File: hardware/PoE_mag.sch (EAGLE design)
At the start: 124 parts, among them IC1 LD1117V33, IC10 PCA9517A, IC11 LD1117V33, IC2 DS1338, IC3 74LVC1T45SOT23-HAND, IC4 ATMEGA1284, IC5 MCP2200, IC6 TSR 1-2450, IC7 74LVC1T45SOT23-HAND, IC8 74LVC1T45SOT23-HAND, IC9 74LVC1T45SOT23-HAND, Q1 BSS138, Q3 BUK98150-55A, X1 PWR, X2 JTAG, X3 USB, X4 CONN-SMATHD, X5 UFL, X6 MICRO-SD-SOCKETHIROSE-DM3D, X7 RJ45, X8 RJ11, X9 22-23-2021, Y1 32k768, Y2 16MHz, Y3 12MHz

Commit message: Version before routing, and possible final routing
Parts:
- removed JP12: 5V LINK, SparkFun:JUMPER-2PTH
- removed JP13: MAG VCC, SparkFun:JUMPER-3PTH
- removed Q3: BUK98150-55A, SteveMarple:FET-N-TYPESOT223-HAND
- added JP2: ISP VCC, SparkFun:JUMPER-2PTH
- added JP3: SQW, SparkFun:JUMPER-3PTH
- added Q2: BUK98150-55A, SteveMarple:FET-N-TYPESOT223-HAND
- C10: value 22p -> 4u7; device SteveMarple:C-EU0805-HAND -> SparkFun:CAP_POLPTH2; OPTION Do not fit for ceramic resonator -> (none)
- C11: value 22p -> 100n; device SteveMarple:C-EU0805-HAND -> SteveMarple:C-EU1206-HAND; OPTION Do not fit for ceramic resonator -> (none)
- C12, C33, C36: value 100n -> 1u
- C13: value 10n -> 22p; device SteveMarple:C-EU1206-HAND -> SteveMarple:C-EU0805-HAND; OPTION (none) -> Do not fit for ceramic resonator
- C14: value 100n -> 22p; device SteveMarple:C-EU1206-HAND -> SteveMarple:C-EU0805-HAND; OPTION (none) -> Do not fit for ceramic resonator
- C15, C16, C21, C22, C28: value 22p -> 100n; device SteveMarple:C-EU0805-HAND -> SteveMarple:C-EU1206-HAND
- C17: value 15p -> 10n; device SteveMarple:C-EU0805-HAND -> SteveMarple:C-EU1206-HAND
- C18: value 15p -> 100n; device SteveMarple:C-EU0805-HAND -> SteveMarple:C-EU1206-HAND
- C19, C20, C34, C35: value 100n -> 22p; device SteveMarple:C-EU1206-HAND -> SteveMarple:C-EU0805-HAND
- C2: value 10u -> 1u; device SteveMarple:CAP_POLPTH2 -> SteveMarple:C-EU1206-HAND
- C27, C29, C39, C8: value 1u -> 100n
- C3: value 100n -> 10u; device SteveMarple:C-EU1206-HAND -> SteveMarple:CAP_POLPTH2
- C31: value 1u -> 22p; device SteveMarple:C-EU1206-HAND -> SteveMarple:C-EU0805-HAND
- C32: value 4u7 -> 1u; device SteveMarple:CAP_POLPTH2 -> SteveMarple:C-EU1206-HAND
- C37: value 100n -> 4u7; device SteveMarple:C-EU1206-HAND -> SteveMarple:CAP_POLPTH2
- C4: value 100p -> 15p; device SteveMarple:C-EU1206-HAND -> SteveMarple:C-EU0805-HAND
- C5: value 100n -> 15p; device SteveMarple:C-EU1206-HAND -> SteveMarple:C-EU0805-HAND
- C6: value 4u7 -> 100n; device SparkFun:CAP_POLPTH2 -> SteveMarple:C-EU1206-HAND
- C7: value 100n -> 100p
- D3: value BAS40 -> BAS21; device SteveMarple:DIODE-SCHOTTKYSOT23-1-3-HAND -> SteveMarple:DIODESOT23-1-3-HAND
- D4: value BAS21 -> BAS40; device SteveMarple:DIODESOT23-1-3-HAND -> SteveMarple:DIODE-SCHOTTKYSOT23-1-3-HAND
- IC1: device SteveMarple:V_REG_LD1117VXXTO220 -> SteveMarple:V_REG_LD1117VXXSOT223-HAND
- IC10: value PCA9517A -> 74LVC1T45SOT23-HAND; device SteveMarple:PCA9517ASOIC -> SteveMarple:74LVC1T45SOT23-HAND
- IC11: value LD1117V33 -> PCA9517A; device SteveMarple:V_REG_LD1117VXXSOT223-HAND -> SteveMarple:PCA9517ASOIC
- IC2: value DS1338 -> LD1117V33; device SteveMarple:DS1307SO08 -> SteveMarple:V_REG_LD1117VXXTO220
- IC3: value 74LVC1T45SOT23-HAND -> DS1338; device SteveMarple:74LVC1T45SOT23-HAND -> SteveMarple:DS1307SO08
- IC5: value MCP2200 -> TSR 1-2450; device SteveMarple:MCP2200 -> PoE_lib:V_REG_78XXTSR/POWERPAX
- IC6: value TSR 1-2450 -> MCP2200; device PoE_lib:V_REG_78XXTSR/POWERPAX -> SteveMarple:MCP2200
- JP1: value SQW -> 3V3/5V
- JP10: value CONFIG -> 5V LINK; device pinhead:PINHD-2X5 -> SparkFun:JUMPER-2PTH
- JP11: value GPS !RESET! (A0) -> MAG VCC; device SparkFun:JUMPER-2PTH -> SparkFun:JUMPER-3PTH
- JP4: value PPS -> USB/VIN
- JP5: value 3V3/5V -> AUTO RST; device SparkFun:JUMPER-3PTH -> SparkFun:JUMPER-2PTH
- JP6: value V ANT -> GPS !RESET! (A0); device SparkFun:JUMPER-3PTH -> SparkFun:JUMPER-2PTH
- JP7: value AUTO RST -> V ANT; device SparkFun:JUMPER-2PTH -> SparkFun:JUMPER-3PTH
- JP8: value ISP VCC -> CONFIG; device SparkFun:JUMPER-2PTH -> pinhead:PINHD-2X5
- JP9: value USB/VIN -> PPS
- R10: value 1M -> 1k
- R18: value 3k 1% -> 330R
- R19: value 1k 1% -> 1M
- R20: value 1M -> 3k 1%
- R21: value 330R -> 1k 1%
- R3: value 10k -> 1M
- R4: value 4k7 -> 10k
- R6: value 10k -> 4k7
- R7: value 1k -> 10k
- U$5: value ? -> PAD
- U$8: value PAD -> ?
- X4: value CONN-SMATHD -> MICRO-SD-SOCKETHIROSE-DM3D; device SteveMarple:CONN-SMATHD -> SteveMarple:MICRO-SD-SOCKETHIROSE-DM3D
- X5: value UFL -> CONN-SMATHD; device SteveMarple:CONN-UFLHAND -> SteveMarple:CONN-SMATHD
- X6: value MICRO-SD-SOCKETHIROSE-DM3D -> UFL; device SteveMarple:MICRO-SD-SOCKETHIROSE-DM3D -> SteveMarple:CONN-UFLHAND
- X7: value RJ45 -> 22-23-2021; device SteveMarple:RJ45-8PTH -> con-molex:22-23-2021
- X8: value RJ11 -> RJ45; device SteveMarple:RJ11-6PTH -> SteveMarple:RJ45-8PTH
- X9: value 22-23-2021 -> RJ11; device con-molex:22-23-2021 -> SteveMarple:RJ11-6PTH
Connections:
- net !GPS_RESET: now also IC7.A; no longer IC8.A
- net !MCP2200_RESET: now also IC6.!RST, R10.1; no longer IC5.!RST, R9.1
- net !RESET: now also C21.2, R7.1; no longer C12.2, R6.1
- net +3V3: now also C16.1, C3.+, C31.1, C32.1, C33.1, IC10.VCC_B, IC2.OUT, IC6.VUSB, JP1.1, JP11.3, JP7.3, JP8.2, JP8.4, JP8.6, U$3.1; no longer C19.1, C2.+, C25.1, C35.1, C36.1, IC11.OUT, IC3.VCC_B, IC5.VUSB, JP10.2, JP10.4, JP10.6, JP13.3, JP5.1, JP6.3, U$11.1
- net +5V: now also C2.1, IC2.IN, JP1.3, JP10.1, JP4.2, JP7.1, U$4.1; no longer C39.1, IC11.IN, JP12.1, JP5.3, JP6.1, JP9.2, U$12.1
- net +5V_USB: now also C17.1, JP4.3; no longer C13.1, JP9.3
- net 0(RX0): now also IC6.TX; no longer IC5.TX
- net 1(TX0): now also IC6.RX; no longer IC5.RX
- net 11(MOSI): now also X4.CMD; no longer X6.CMD
- net 12(MISO): now also X4.DAT0; no longer X6.DAT0
- net 13(SCK): now also R3.2, X4.CLK; no longer R10.2, X6.CLK
- net 15: now also JP3.1; no longer JP1.1
- net 20(SDA): now also IC11.SDA_A, IC3.SDA, R14.1, R6.1; no longer IC10.SDA_A, IC2.SDA, R15.1, R5.1
- net 21(SCL): now also IC11.SCL_A, IC3.SCL, R15.1, R5.1; no longer IC10.SCL_A, IC2.SCL, R14.1, R4.1
- net 22: now also X4.CD/DAT3; no longer X6.CD/DAT3
- net 3(TX1): now also IC8.B; no longer IC7.B
- net 6: now also JP3.3, JP9.3; no longer JP1.3, JP4.3
- net 7: now also JP9.1; no longer JP4.1
- net 8: now also R18.1; no longer R21.1
- net A0: now also JP6.1; no longer JP11.1
- net A2: now also D4.A, R20.2, R21.2; no longer D3.A, R18.2, R19.2
- net AREF: now also C8.1; no longer C5.1
- net AUTO_RESET: now also IC6.!RTS, JP5.1; no longer IC5.!RTS, JP7.1
- net AVCC: now also C11.1; no longer C9.1
- net FAN_CTRL: now also D3.C, Q2.D, X7-2.S; no longer D4.C, Q3.D, X9-2.S
- net GND: now also C10.-, C12.2, C2.2, C3.-, C32.2, C37.-, C6.2, D3.A, IC10.DIR, IC5.GND, IC6.VSS, JP8.10, JP8.8, Q2.S, R21.1, R3.1, U$2.1, X4.SHIELD, X4.VSS, X6.GND, X8.4, X9.2, X9.3; no longer C10.2, C2.-, C3.2, C32.-, C34.2, C37.2, C6.-, D4.A, IC3.DIR, IC5.VSS, IC6.GND, JP10.10, JP10.8, Q3.S, R10.1, R20.1, U$13.1, X4.GND, X6.SHIELD, X6.VSS, X7.3, X7.4, X8.2
- net GPIO0: now also U$6.1; no longer U$3.1
- net GPIO1: now also IC10.B, U$7.1; no longer IC9.B, U$4.1
- net GPIO2: now also U$8.1; no longer U$5.1
- net GPIO3: now also JP8.1, U$9.1; no longer JP10.1, U$6.1
- net GPIO4: now also JP8.3, U$10.1; no longer JP10.3, U$7.1
- net GPIO5: now also JP8.5, U$11.1; no longer JP10.5, U$8.1
- net GPIO6: now also JP8.7, U$12.1; no longer JP10.7, U$9.1
- net GPIO7: now also JP8.9, U$13.1; no longer JP10.9, U$10.1
- net GPS_RX1: now also IC8.A; no longer IC7.A
- net GPS_TX1: now also IC9.B; no longer IC3.B
- net MAG_SCL: now also IC11.SCL_B, X8.5, X9.4; no longer IC10.SCL_B, X7.5, X8.4
- net MAG_SDA: now also IC11.SDA_B, X8.7, X9.6; no longer IC10.SDA_B, X7.7, X8.6
- net MAG_VCC: now also C39.1, IC11.EN, IC11.VCC_B, JP10.2, X8.6, X9.5; no longer C37.1, IC10.EN, IC10.VCC_B, JP12.2, X7.6, X8.5
- net N$1: now also C14.1; no longer C11.1
- net N$11: now also C7.1, IC3.VBATT, R9.2; no longer C4.1, IC2.VBATT, R7.2
- net N$12: now also C5.1, IC3.X2; no longer C17.1, IC2.X2
- net N$14: now also IC5.OUT, JP4.1; no longer IC6.OUT, JP9.1
- net N$15: now also C21.1, JP5.2; no longer C12.1, JP7.2
- net N$18: now also C19.1, IC6.OSC1; no longer C15.1, IC5.OSC1
- net N$2: now also C13.1; no longer C10.1
- net N$22: now also IC7.B, JP6.2; no longer IC8.B, JP11.2
- net N$23: now also C34.2, X6.SIGNAL; no longer C21.2, X4.SIGNAL
- net N$24: now also C34.1; no longer C21.1
- net N$25: now also IC9.A; no longer IC3.A
- net N$26: now also JP11.2, X8.8; no longer JP13.2, X7.8
- net N$29: now also Q2.G, R18.2, R19.2; no longer Q3.G, R20.2, R21.2
- net N$5: now also C4.1, IC3.X1; no longer C18.1, IC2.X1
- net N$6: now also JP2.1; no longer JP8.1
- net N$7: now also C20.1, IC6.OSC2; no longer C16.1, IC5.OSC2
- net N$9: now also R9.1; no longer R7.1
- net PPS: now also IC10.A, JP9.2; no longer IC9.A, JP4.2
- net SLEEP_FLAG: now also U$5.1; no longer U$2.1
- net SQW: now also IC3.SQW, JP3.2, R4.1; no longer IC2.SQW, JP1.2, R3.1
- net USB_D+: now also IC6.D+; no longer IC5.D+
- net USB_D-: now also IC6.D-; no longer IC5.D-
- net VCC: now also C10.+, C15.1, C18.1, C22.1, C25.1, C6.1, C9.1, D4.C, IC11.VCC_A, IC3.VCC, IC6.VDD, JP1.2, JP2.2, R10.2, R7.2, X4.VDD; no longer C14.1, C20.1, C3.1, C33.1, C34.1, C6.+, C7.1, D3.C, IC2.VCC, IC3.VCC_A, IC5.VDD, JP5.2, JP8.2, R3.2, R9.2, X6.VDD
- net VIN: now also C12.1, IC5.IN, JP11.1, R20.1, X7-1.S, X8.2, X9.1; no longer C8.1, IC6.IN, JP13.1, R18.1, X7.2, X8.1, X9-1.S
- net V_ANT: now also C35.1, C36.1, C37.+, JP7.2; no longer C22.1, C31.1, C32.+, JP6.2
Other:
- note removed: "2.1"
- note removed: "TODO Add TO-220 option for LD-1117"
- note removed: "TODO Swap MCP1702 (3V3 and 5V) for SMD"

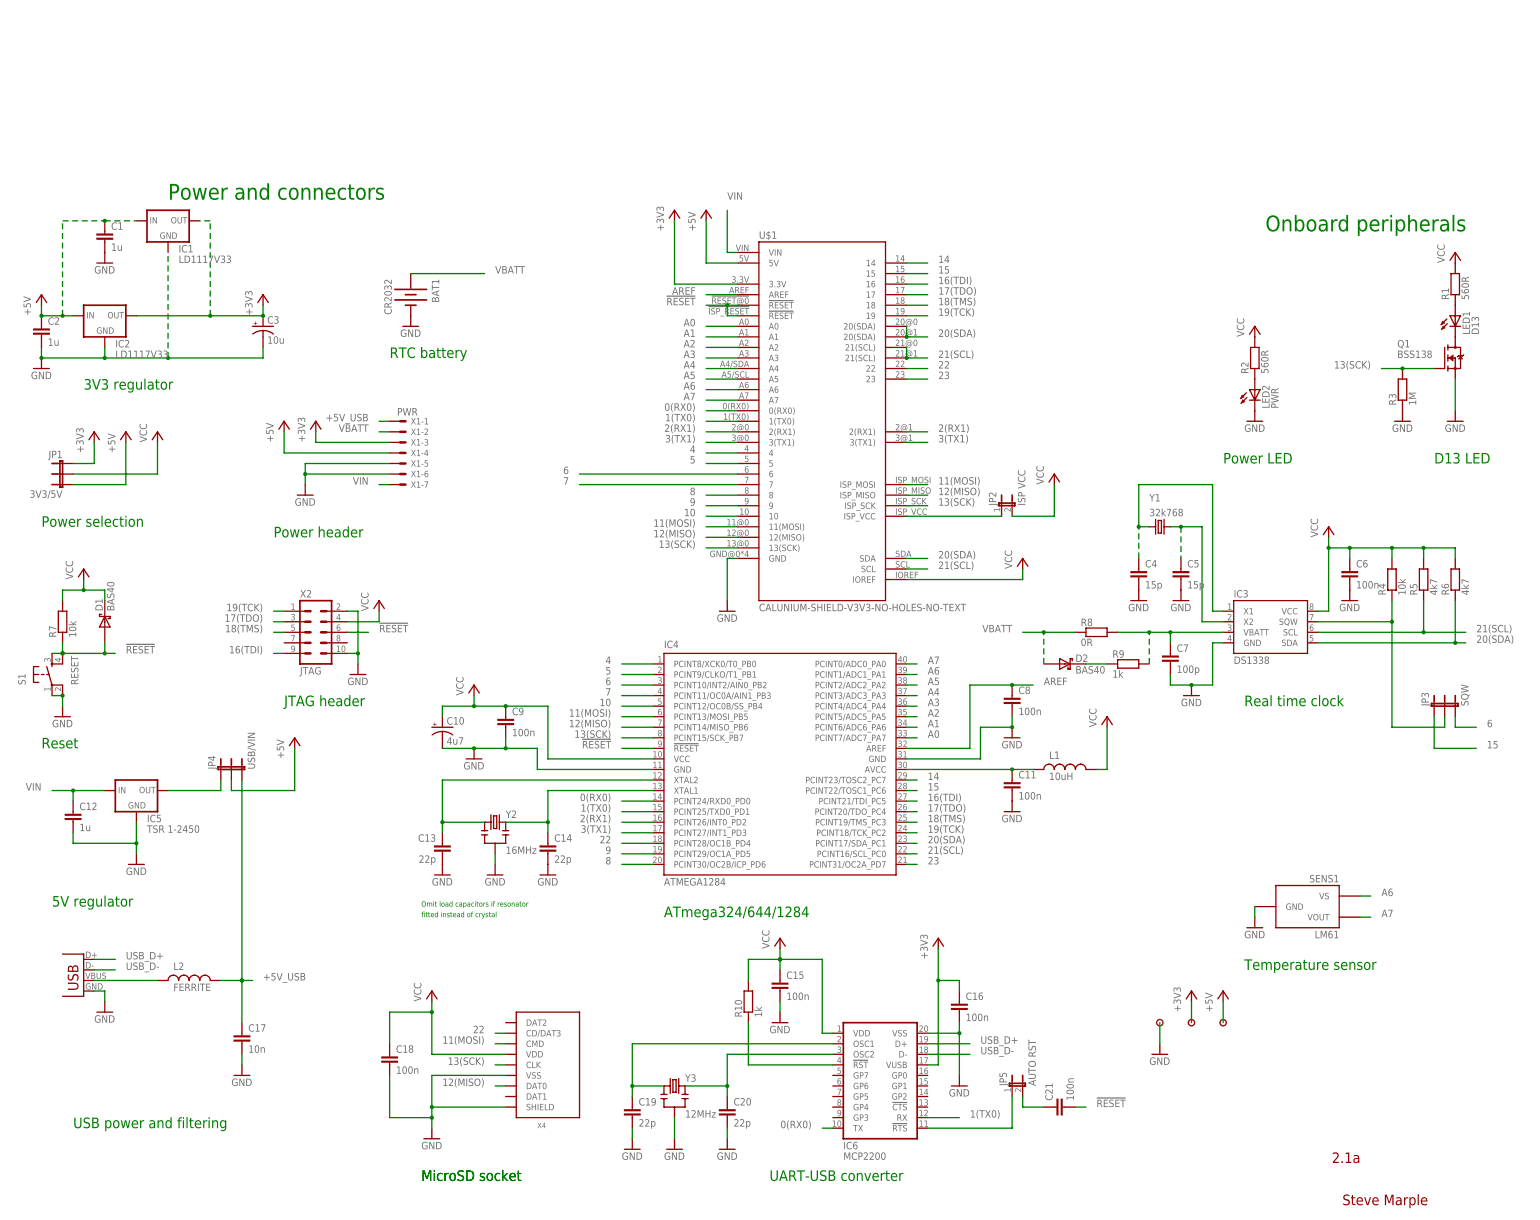
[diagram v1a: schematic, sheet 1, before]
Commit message: Fix incorrect USB power filtering
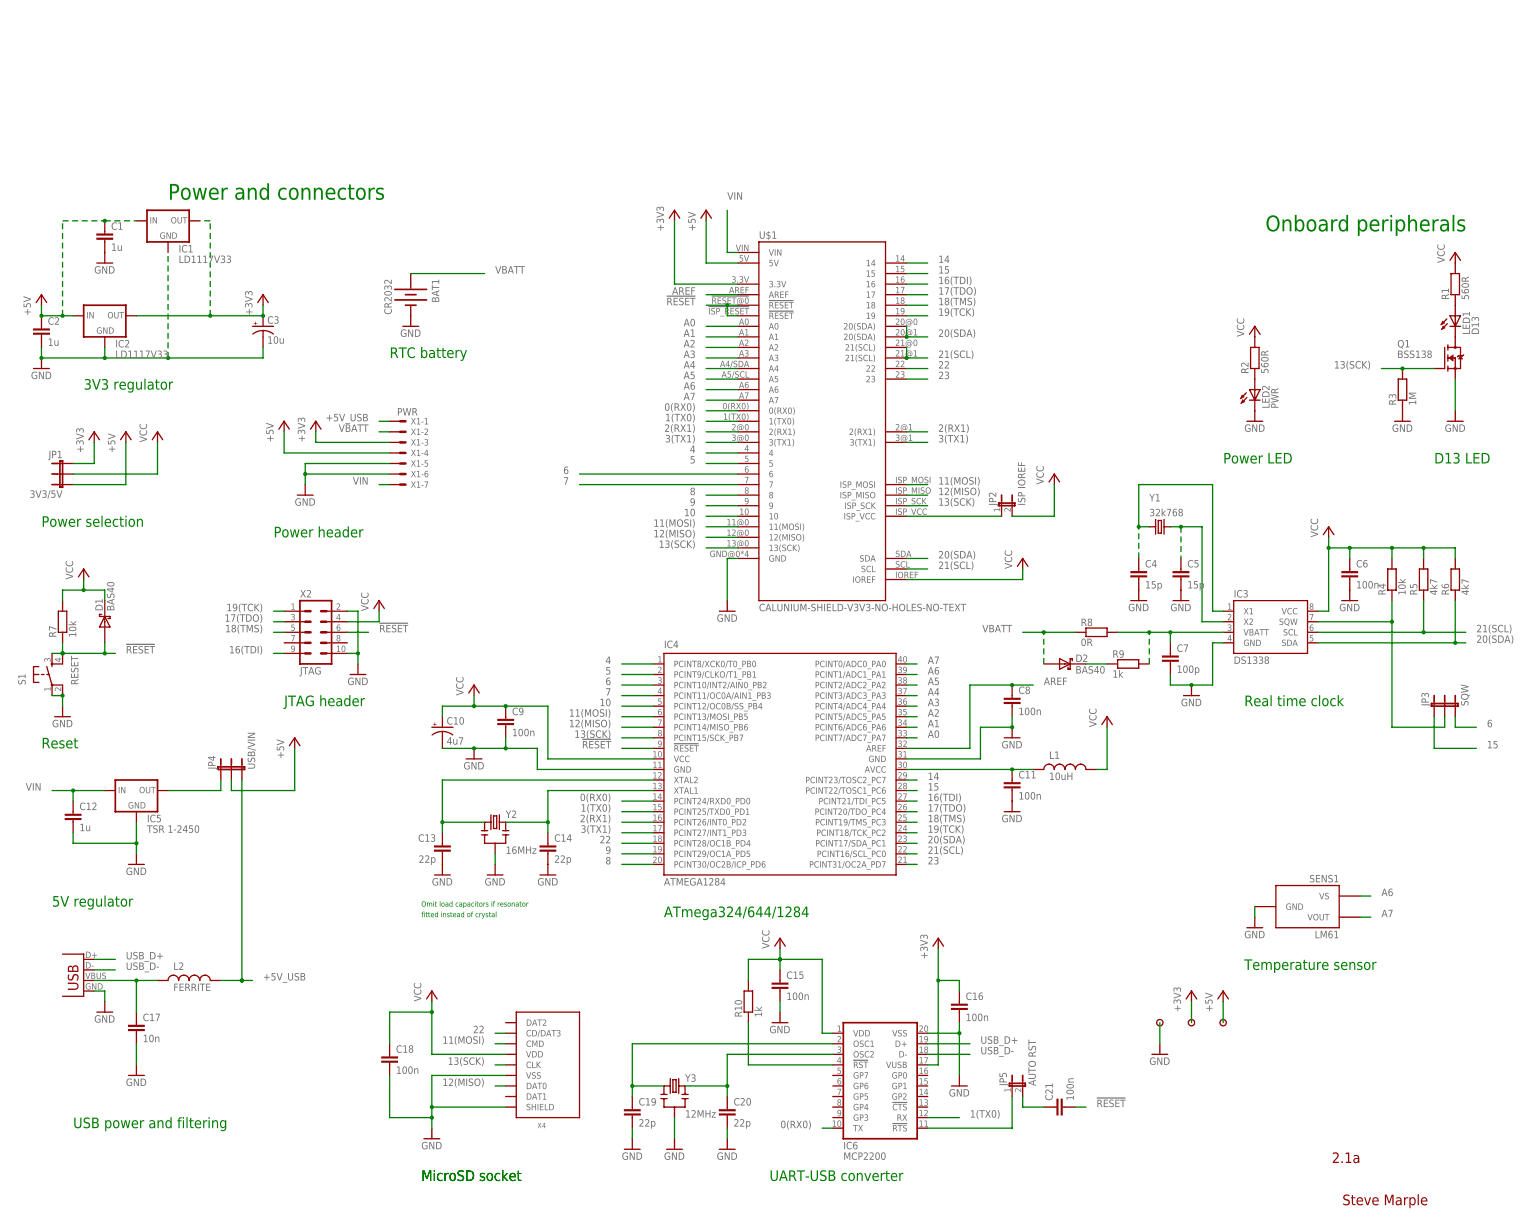
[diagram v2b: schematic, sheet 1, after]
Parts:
- JP2: value ISP VCC -> ISP IOREF
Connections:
- net +5V_USB: no longer C17.1
- net VBUS: now also C17.1
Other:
- moved on the sheet: C17
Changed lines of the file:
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@@
 <part name="P+23" library="supply1" deviceset="VCC" device=""/>
 <part name="GND32" library="supply1" deviceset="GND" device=""/>
-<part name="JP2" library="SparkFun" deviceset="JUMPER-2" device="PTH" value="ISP VCC"/>
+<part name="JP2" library="SparkFun" deviceset="JUMPER-2" device="PTH" value="ISP IOREF"/>
 <part name="JP3" library="SparkFun" deviceset="JUMPER-3" device="PTH" value="SQW"/>
 <part name="R8" library="SteveMarple" deviceset="RESISTOR" device="1206-HAND" value="0R"/>
@@
 <instance part="R8" gate="G$1" x="99.06" y="66.04"/>
 <instance part="L2" gate="G$1" x="-119.38" y="-17.78"/>
-<instance part="GND7" gate="1" x="-106.68" y="-40.64"/>
-<instance part="C17" gate="G$1" x="-106.68" y="-30.48"/>
+<instance part="GND7" gate="1" x="-132.08" y="-40.64"/>
+<instance part="C17" gate="G$1" x="-132.08" y="-27.94"/>
 <instance part="C16" gate="G$1" x="66.04" y="-22.86"/>
 <instance part="C15" gate="G$1" x="22.86" y="-17.78"/>
@@
 <pinref part="C17" gate="G$1" pin="2"/>
 <pinref part="GND7" gate="1" pin="GND"/>
-<wire x1="-106.68" y1="-38.1" x2="-106.68" y2="-35.56" width="0.1524" layer="91"/>
+<wire x1="-132.08" y1="-38.1" x2="-132.08" y2="-33.02" width="0.1524" layer="91"/>
 </segment>
 <segment>
@@
 <label x="-101.6" y="-17.78" size="1.778" layer="95"/>
 <junction x="-106.68" y="-17.78"/>
-<pinref part="C17" gate="G$1" pin="1"/>
-<wire x1="-106.68" y1="-27.94" x2="-106.68" y2="-17.78" width="0.1524" layer="91"/>
 <pinref part="JP4" gate="G$1" pin="3"/>
 <junction x="-106.68" y="-17.78"/>
@@
 </segment>
 </net>
-<net name="N$14" class="0">
+<net name="N$14" class="1">
 <segment>
 <pinref part="IC5" gate="G$1" pin="OUT"/>
@@
 <pinref part="X3" gate="G$1" pin="VBUS"/>
 <pinref part="L2" gate="G$1" pin="1"/>
-<wire x1="-127" y1="-17.78" x2="-142.24" y2="-17.78" width="0.1524" layer="91"/>
+<wire x1="-127" y1="-17.78" x2="-132.08" y2="-17.78" width="0.1524" layer="91"/>
+<junction x="-132.08" y="-17.78"/>
+<wire x1="-132.08" y1="-17.78" x2="-142.24" y2="-17.78" width="0.1524" layer="91"/>
+<pinref part="C17" gate="G$1" pin="1"/>
+<wire x1="-132.08" y1="-17.78" x2="-132.08" y2="-25.4" width="0.1524" layer="91"/>
 </segment>
 </net>
@@
 </segment>
 </net>
-<net name="MAG_VCC" class="0">
+<net name="MAG_VCC" class="1">
 <segment>
 <pinref part="IC11" gate="G$1" pin="VCC_B"/>

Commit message: Routed layout with no DRC warnings
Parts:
- LED1, LED2: device SparkFun:LED3MM -> PoE_lib:LED3MM
- X1: device con-molex:22-23-2071 -> PoE_lib:22-23-2071
- X7: device con-molex:22-23-2021 -> PoE_lib:22-23-2021
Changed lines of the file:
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@@
 <part name="Q1" library="SteveMarple" deviceset="BSS138" device="SOT23-3-HAND" value="BSS138"/>
 <part name="IC3" library="SteveMarple" deviceset="DS1307" device="SO08" value="DS1338"/>
-<part name="LED1" library="SparkFun" deviceset="LED" device="3MM" value="D13"/>
-<part name="LED2" library="SparkFun" deviceset="LED" device="3MM" value="PWR"/>
+<part name="LED1" library="PoE_lib" deviceset="LED" device="3MM" value="D13"/>
+<part name="LED2" library="PoE_lib" deviceset="LED" device="3MM" value="PWR"/>
 <part name="R1" library="SteveMarple" deviceset="RESISTOR" device="1206-HAND" value="560R"/>
 <part name="Y1" library="SteveMarple" deviceset="CRYSTAL" device="TC38H" value="32k768"/>
@@
 <part name="GND4" library="supply1" deviceset="GND" device=""/>
 <part name="C10" library="SparkFun" deviceset="CAP_POL" device="PTH2" value="4u7"/>
-<part name="X1" library="con-molex" deviceset="22-23-2071" device="" value="PWR"/>
+<part name="X1" library="PoE_lib" deviceset="22-23-2071" device="" value="PWR"/>
 <part name="GND5" library="supply1" deviceset="GND" device=""/>
 <part name="P+4" library="supply1" deviceset="+5V" device=""/>
@@
 <part name="D3" library="SteveMarple" deviceset="DIODE" device="SOT23-1-3-HAND" value="BAS21"/>
 <part name="GND48" library="supply1" deviceset="GND" device=""/>
-<part name="X7" library="con-molex" deviceset="22-23-2021" device=""/>
+<part name="X7" library="PoE_lib" deviceset="22-23-2021" device=""/>
 <part name="BOX1" library="fibox" deviceset="BOX" device="POE-MAG-150-150" value="BOXPOE-MAG-150-150"/>
 <part name="Q2" library="SteveMarple" deviceset="FET-N-TYPE" device="SOT223-HAND" value="BUK98150-55A"/>
